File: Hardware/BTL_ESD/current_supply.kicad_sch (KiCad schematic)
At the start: 1 part, among them U5 MCP6002-xSN

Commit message: hardware: ver 1 schematic
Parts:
- removed U5: MCP6002-xSN, symbol Amplifier_Operational:MCP6002-xSN
- added C44, C45: 10uF/16V, Capacitor_SMD:C_0603_1608Metric_Pad1.08x0.95mm_HandSolder, symbol Device:C_Small
- added C46, C47: 100nF/16V, Capacitor_SMD:C_0603_1608Metric_Pad1.08x0.95mm_HandSolder, symbol Device:C_Small
- added R19, R20, R21, R22: 100k/1%, Resistor_SMD:R_0603_1608Metric_Pad0.98x0.95mm_HandSolder, symbol Device:R_US
- added R23: 200k/1%, Resistor_SMD:R_0603_1608Metric_Pad0.98x0.95mm_HandSolder, symbol Device:R_US
- added U6: MCP6002-E_SN, MCP6002-E_SN:SOIC127P599X175-8N, symbol MCP6002-E_SN:MCP6002-E_SN
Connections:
- new net: R19.2, R23.1, U6.2 (VINA-)
- new net: R20.2, R21.1, U6.3 (VINA+)
- new net: R22.2, R23.2, U6.1 (VOUTA)
- new net +5V: C44.1, C46.1, R20.1, U6.8 (VDD)
- new net -5V: C45.1, C47.1, U6.4 (VSS)
- new net CURRENT_SUPPLY: R21.2, R22.1
- new net GND: C44.2, C45.2, C46.2, C47.2, R19.1
- no-connect marks 0 -> 3
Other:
- title: (none) -> CURRENT SUPPLY

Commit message: update
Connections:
- net GND renamed GNDA
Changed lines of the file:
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@@
+    )
+  )
+  (symbol (lib_id "power:GNDA") (at 222.25 77.47 0) (unit 1)
+    (in_bom yes) (on_board yes) (dnp no) (fields_autoplaced)
+    (property "Reference" "#PWR059" (at 222.25 83.82 0)
+      (effects (font (size 1.27 1.27)) hide)
+    )
+    (property "Value" "GNDA" (at 222.25 82.55 0)
+      (effects (font (size 1.27 1.27)))
+    )
+    (property "Footprint" "" (at 222.25 77.47 0)
+      (effects (font (size 1.27 1.27)) hide)
+    )
+    (property "Datasheet" "" (at 222.25 77.47 0)
+      (effects (font (size 1.27 1.27)) hide)
+    )
+    (pin "1")
+    (instances
+      (project "BTL_ESD"
+        (path "/ce4779b4-6d78-42e3-84df-0a4e77629b0f/5e78f83c-f202-4ca3-bd35-bb95a1f1b22b"
+          (reference "#PWR059") (unit 1)
+        )
+      )
     )
   )
@@
         (path "/ce4779b4-6d78-42e3-84df-0a4e77629b0f/5e78f83c-f202-4ca3-bd35-bb95a1f1b22b"
           (reference "#PWR060") (unit 1)
-        )
-      )
-    )
-  )
-  (symbol (lib_id "power:GND") (at 92.71 113.03 0) (unit 1)
-    (in_bom yes) (on_board yes) (dnp no) (fields_autoplaced)
-    (property "Reference" "#PWR054" (at 92.71 119.38 0)
-      (effects (font (size 1.27 1.27)) hide)
-    )
-    (property "Value" "GND" (at 92.71 118.11 0)
-      (effects (font (size 1.27 1.27)))
-    )
-    (property "Footprint" "" (at 92.71 113.03 0)
-      (effects (font (size 1.27 1.27)) hide)
-    )
-    (property "Datasheet" "" (at 92.71 113.03 0)
-      (effects (font (size 1.27 1.27)) hide)
-    )
-    (pin "1")
-    (instances
-      (project "BTL_ESD"
-        (path "/ce4779b4-6d78-42e3-84df-0a4e77629b0f/5e78f83c-f202-4ca3-bd35-bb95a1f1b22b"
-          (reference "#PWR054") (unit 1)
-        )
-      )
-    )
-  )
-  (symbol (lib_id "power:GND") (at 222.25 113.03 0) (unit 1)
-    (in_bom yes) (on_board yes) (dnp no) (fields_autoplaced)
-    (property "Reference" "#PWR061" (at 222.25 119.38 0)
-      (effects (font (size 1.27 1.27)) hide)
-    )
-    (property "Value" "GND" (at 222.25 118.11 0)
-      (effects (font (size 1.27 1.27)))
-    )
-    (property "Footprint" "" (at 222.25 113.03 0)
-      (effects (font (size 1.27 1.27)) hide)
-    )
-    (property "Datasheet" "" (at 222.25 113.03 0)
-      (effects (font (size 1.27 1.27)) hide)
-    )
-    (pin "1")
-    (instances
-      (project "BTL_ESD"
-        (path "/ce4779b4-6d78-42e3-84df-0a4e77629b0f/5e78f83c-f202-4ca3-bd35-bb95a1f1b22b"
-          (reference "#PWR061") (unit 1)
-        )
-      )
-    )
-  )
-  (symbol (lib_id "power:GND") (at 222.25 77.47 0) (unit 1)
-    (in_bom yes) (on_board yes) (dnp no) (fields_autoplaced)
-    (property "Reference" "#PWR059" (at 222.25 83.82 0)
-      (effects (font (size 1.27 1.27)) hide)
-    )
-    (property "Value" "GND" (at 222.25 82.55 0)
-      (effects (font (size 1.27 1.27)))
-    )
-    (property "Footprint" "" (at 222.25 77.47 0)
-      (effects (font (size 1.27 1.27)) hide)
-    )
-    (property "Datasheet" "" (at 222.25 77.47 0)
-      (effects (font (size 1.27 1.27)) hide)
-    )
-    (pin "1")
-    (instances
-      (project "BTL_ESD"
-        (path "/ce4779b4-6d78-42e3-84df-0a4e77629b0f/5e78f83c-f202-4ca3-bd35-bb95a1f1b22b"
-          (reference "#PWR059") (unit 1)
         )
       )
@@
     )
   )
+  (symbol (lib_id "power:GNDA") (at 222.25 113.03 0) (unit 1)
+    (in_bom yes) (on_board yes) (dnp no) (fields_autoplaced)
+    (property "Reference" "#PWR061" (at 222.25 119.38 0)
+      (effects (font (size 1.27 1.27)) hide)
+    )
+    (property "Value" "GNDA" (at 222.25 118.11 0)
+      (effects (font (size 1.27 1.27)))
+    )
+    (property "Footprint" "" (at 222.25 113.03 0)
+      (effects (font (size 1.27 1.27)) hide)
+    )
+    (property "Datasheet" "" (at 222.25 113.03 0)
+      (effects (font (size 1.27 1.27)) hide)
+    )
+    (pin "1")
+    (instances
+      (project "BTL_ESD"
+        (path "/ce4779b4-6d78-42e3-84df-0a4e77629b0f/5e78f83c-f202-4ca3-bd35-bb95a1f1b22b"
+          (reference "#PWR061") (unit 1)
+        )
+      )
+    )
+  )
   (symbol (lib_id "Device:C_Small") (at 214.63 71.12 0) (unit 1)
     (in_bom yes) (on_board yes) (dnp no) (fields_autoplaced)
@@
         )
       )
+    )
+  )
+  (symbol (lib_id "power:GNDA") (at 92.71 113.03 0) (unit 1)
+    (in_bom yes) (on_board yes) (dnp no) (fields_autoplaced)
+    (property "Reference" "#PWR054" (at 92.71 119.38 0)
+      (effects (font (size 1.27 1.27)) hide)
+    )
+    (property "Value" "GNDA" (at 92.71 118.11 0)
+      (effects (font (size 1.27 1.27)))
+    )
+    (property "Footprint" "" (at 92.71 113.03 0)
+      (effects (font (size 1.27 1.27)) hide)
+    )
+    (property "Datasheet" "" (at 92.71 113.03 0)
+      (effects (font (size 1.27 1.27)) hide)
+    )
+    (pin "1")
+    (instances
+      (project "BTL_ESD"
+        (path "/ce4779b4-6d78-42e3-84df-0a4e77629b0f/5e78f83c-f202-4ca3-bd35-bb95a1f1b22b"
+          (reference "#PWR054") (unit 1)
+        )
+      )

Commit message: update
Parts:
- renumbered R19 to R20, R20 to R21, R21 to R22, R22 to R23, R23 to R24

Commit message: fea:STM32: upload structure fodler
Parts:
- renumbered R20 to R21, R21 to R22, R22 to R23, R23 to R24, R24 to R25
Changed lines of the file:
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@@
   (symbol (lib_id "Device:R_US") (at 102.87 111.76 90) (unit 1)
     (in_bom yes) (on_board yes) (dnp no) (fields_autoplaced)
-    (property "Reference" "R20" (at 102.87 105.41 90)
+    (property "Reference" "R21" (at 102.87 105.41 90)
       (effects (font (size 1.27 1.27)))
     )
@@
       (project "BTL_ESD"
         (path "/ce4779b4-6d78-42e3-84df-0a4e77629b0f/5e78f83c-f202-4ca3-bd35-bb95a1f1b22b"
-          (reference "R20") (unit 1)
+          (reference "R21") (unit 1)
         )
       )
@@
   (symbol (lib_id "Device:R_US") (at 120.65 68.58 90) (unit 1)
     (in_bom yes) (on_board yes) (dnp no) (fields_autoplaced)
-    (property "Reference" "R22" (at 120.65 62.23 90)
+    (property "Reference" "R23" (at 120.65 62.23 90)
       (effects (font (size 1.27 1.27)))
     )
@@
       (project "BTL_ESD"
         (path "/ce4779b4-6d78-42e3-84df-0a4e77629b0f/5e78f83c-f202-4ca3-bd35-bb95a1f1b22b"
-          (reference "R22") (unit 1)
+          (reference "R23") (unit 1)
         )
       )
@@
   (symbol (lib_id "Device:R_US") (at 134.62 68.58 90) (unit 1)
     (in_bom yes) (on_board yes) (dnp no) (fields_autoplaced)
-    (property "Reference" "R23" (at 134.62 62.23 90)
+    (property "Reference" "R24" (at 134.62 62.23 90)
       (effects (font (size 1.27 1.27)))
     )
@@
       (project "BTL_ESD"
         (path "/ce4779b4-6d78-42e3-84df-0a4e77629b0f/5e78f83c-f202-4ca3-bd35-bb95a1f1b22b"
-          (reference "R23") (unit 1)
+          (reference "R24") (unit 1)
         )
       )
@@
   (symbol (lib_id "Device:R_US") (at 134.62 111.76 90) (unit 1)
     (in_bom yes) (on_board yes) (dnp no) (fields_autoplaced)
-    (property "Reference" "R24" (at 134.62 105.41 90)
+    (property "Reference" "R25" (at 134.62 105.41 90)
       (effects (font (size 1.27 1.27)))
     )
@@
       (project "BTL_ESD"
         (path "/ce4779b4-6d78-42e3-84df-0a4e77629b0f/5e78f83c-f202-4ca3-bd35-bb95a1f1b22b"
-          (reference "R24") (unit 1)
+          (reference "R25") (unit 1)
         )
       )
@@
   (symbol (lib_id "Device:R_US") (at 104.14 68.58 90) (unit 1)
     (in_bom yes) (on_board yes) (dnp no) (fields_autoplaced)
-    (property "Reference" "R21" (at 104.14 62.23 90)
+    (property "Reference" "R22" (at 104.14 62.23 90)
       (effects (font (size 1.27 1.27)))
     )
@@
       (project "BTL_ESD"
         (path "/ce4779b4-6d78-42e3-84df-0a4e77629b0f/5e78f83c-f202-4ca3-bd35-bb95a1f1b22b"
-          (reference "R21") (unit 1)
-        )
-      )
+          (reference "R22") (unit 1)
+        )
+      )

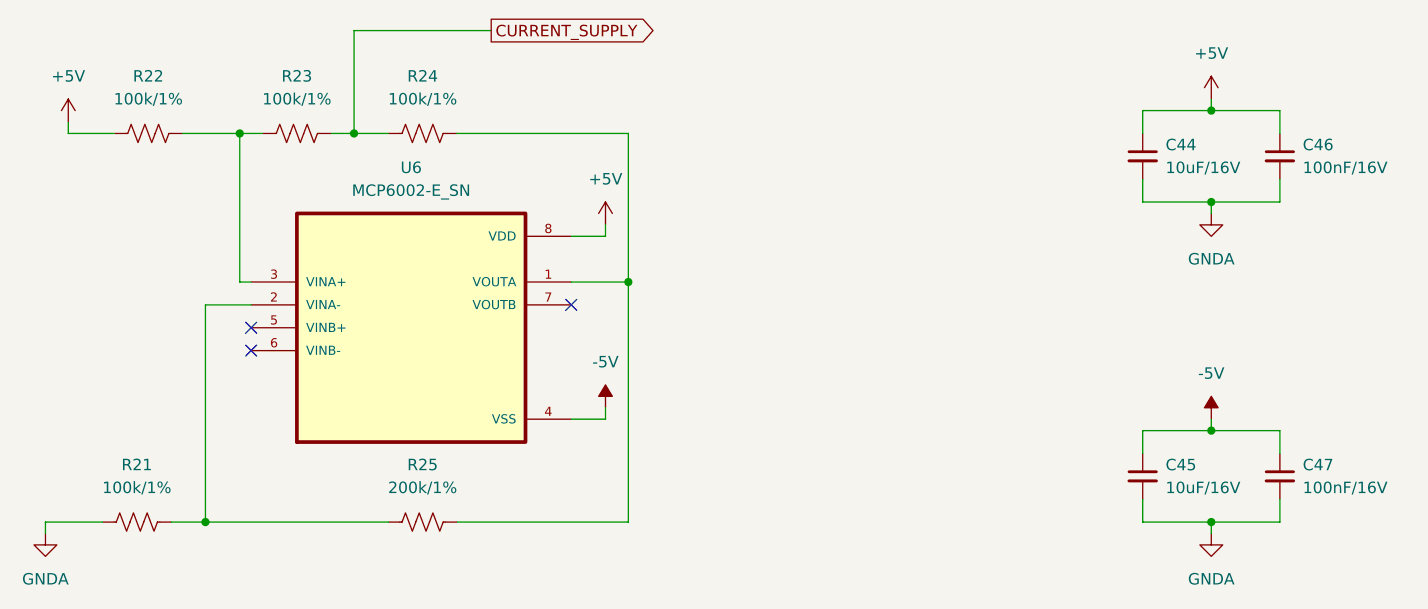
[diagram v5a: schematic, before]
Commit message: code:ESP32: update uart driver, main.c && hardware file pcb
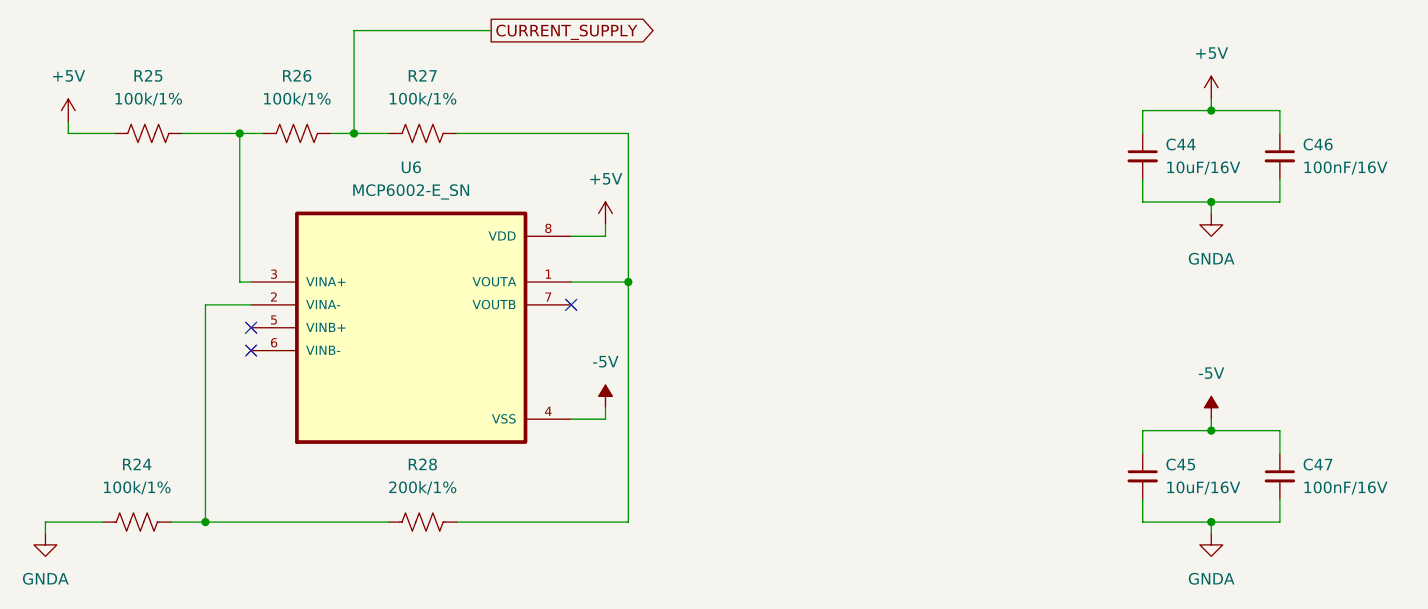
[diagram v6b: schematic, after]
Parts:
- renumbered R21 to R24, R22 to R25, R23 to R26, R24 to R27, R25 to R28
